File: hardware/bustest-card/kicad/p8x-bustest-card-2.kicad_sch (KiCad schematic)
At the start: 2 parts, among them J1 MABC96R, J2 PROBE

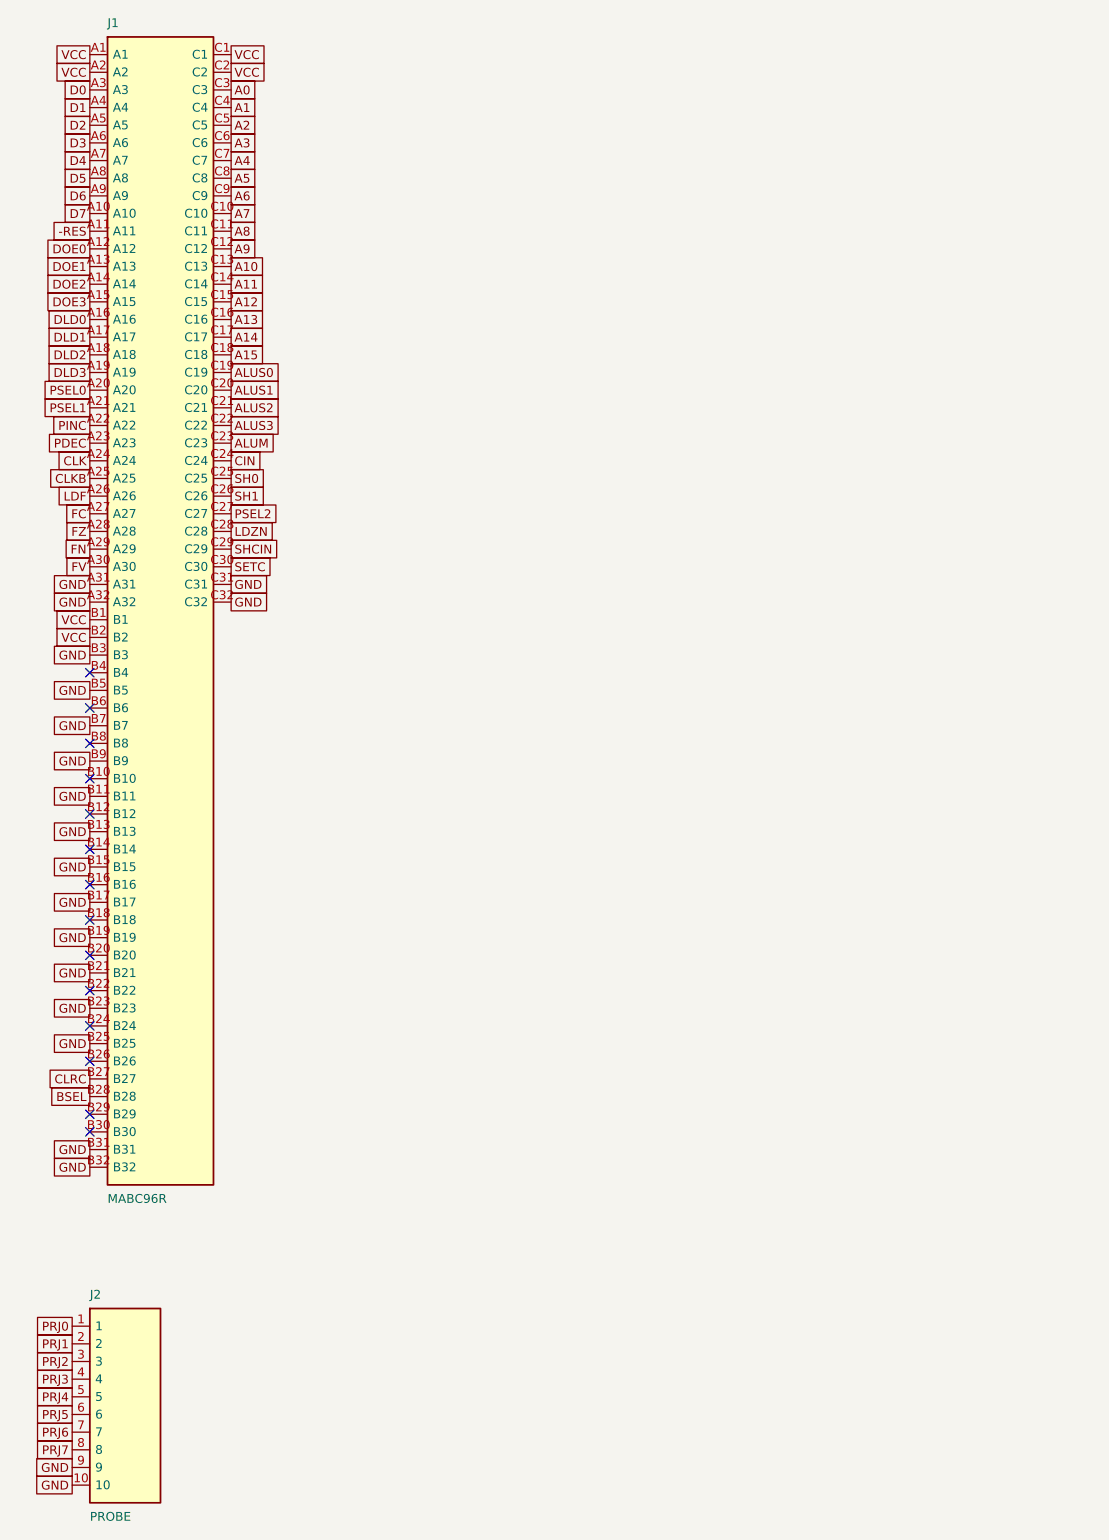
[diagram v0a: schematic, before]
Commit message: feat(sch): draw every P8X card schematic by function
Extend the functional-sheet grouping from the io-card to the control,
regbank, alu, memory, cf, ps2 and bustest cards. functional_sheets now
attaches unnamed glue gates, LEDs, resistors and connectors to the block
they share the most local nets with, so each block lists only its main
parts. A net with two or more pins on a sheet is now wired there even if
it continues elsewhere (its global name label rides on the wire), and
every wire is oriented by drawing side. The regbank gets one pointer per
sheet; the ps2 latches share a sheet with the AVR so the mailbox bus is
drawn. The bustest probe resistors use a straight-order RNISO8DSTR
drawing (the reversed B side forced every wire to cross and the sheet
fell back to labels). build_sch.sh now shows ELK fallbacks and clears old
numbered sheets before a build. All eight netlists match the boards,
ERC 0 errors; the boards change only in footprint link paths.

Co-Authored-By: Claude Opus 5.5 <noreply@anthropic.com>
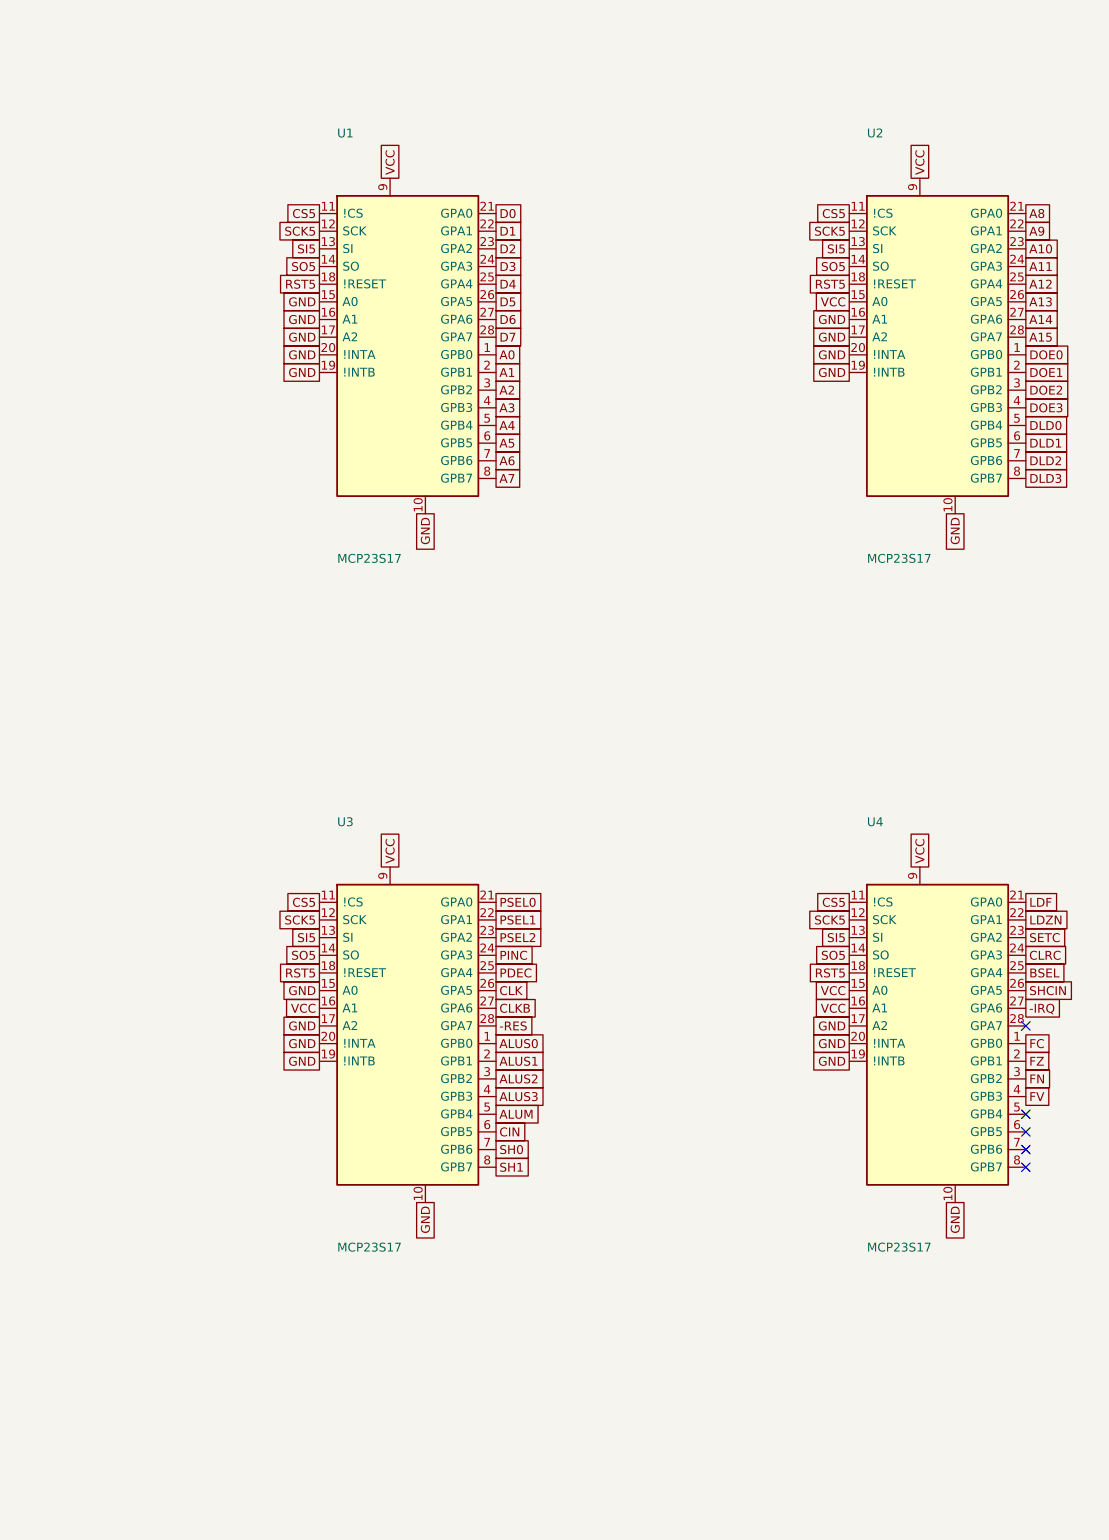
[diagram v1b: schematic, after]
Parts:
- removed J1: MABC96R, Connector_DIN:DIN41612_C_3x32_Male_Horizontal_THT, symbol p8x:DIN96C
- removed J2: PROBE, Connector_PinHeader_2.54mm:PinHeader_1x10_P2.54mm_Vertical, symbol p8x:HDR10
- added U1, U2, U3, U4: MCP23S17, Package_DIP:DIP-28_W7.62mm, symbol p8x:MCP23S17
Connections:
- net -RES: now also U3.28 (GPA7)
- net A0: now also U1.1 (GPB0)
- net A1: now also U1.2 (GPB1)
- net A10: now also U2.23 (GPA2)
- net A11: now also U2.24 (GPA3)
- net A12: now also U2.25 (GPA4)
- net A13: now also U2.26 (GPA5)
- net A14: now also U2.27 (GPA6)
- net A15: now also U2.28 (GPA7)
- net A2: now also U1.3 (GPB2)
- net A3: now also U1.4 (GPB3)
- net A4: now also U1.5 (GPB4)
- net A5: now also U1.6 (GPB5)
- net A6: now also U1.7 (GPB6)
- net A7: now also U1.8 (GPB7)
- net A8: now also U2.21 (GPA0)
- net A9: now also U2.22 (GPA1)
- net ALUM: now also U3.5 (GPB4)
- net ALUS0: now also U3.1 (GPB0)
- net ALUS1: now also U3.2 (GPB1)
- net ALUS2: now also U3.3 (GPB2)
- net ALUS3: now also U3.4 (GPB3)
- net BSEL: now also U4.25 (GPA4)
- net CIN: now also U3.6 (GPB5)
- net CLK: now also U3.26 (GPA5)
- net CLKB: now also U3.27 (GPA6)
- net CLRC: now also U4.24 (GPA3)
- net D0: now also U1.21 (GPA0)
- net D1: now also U1.22 (GPA1)
- net D2: now also U1.23 (GPA2)
- net D3: now also U1.24 (GPA3)
- net D4: now also U1.25 (GPA4)
- net D5: now also U1.26 (GPA5)
- net D6: now also U1.27 (GPA6)
- net D7: now also U1.28 (GPA7)
- net DLD0: now also U2.5 (GPB4)
- net DLD1: now also U2.6 (GPB5)
- net DLD2: now also U2.7 (GPB6)
- net DLD3: now also U2.8 (GPB7)
- net DOE0: now also U2.1 (GPB0)
- net DOE1: now also U2.2 (GPB1)
- net DOE2: now also U2.3 (GPB2)
- net DOE3: now also U2.4 (GPB3)
- net FC: now also U4.1 (GPB0)
- net FN: now also U4.3 (GPB2)
- net FV: now also U4.4 (GPB3)
- net FZ: now also U4.2 (GPB1)
- net GND: now also U1.10, U1.15 (A0), U1.16 (A1), U1.17 (A2), U1.19 (!INTB), U1.20 (!INTA), U2.10, U2.16 (A1), U2.17 (A2), U2.19 (!INTB), U2.20 (!INTA), U3.10, U3.15 (A0), U3.17 (A2), U3.19 (!INTB), U3.20 (!INTA), U4.10, U4.17 (A2), U4.19 (!INTB), U4.20 (!INTA)
- net LDF: now also U4.21 (GPA0)
- net LDZN: now also U4.22 (GPA1)
- net PDEC: now also U3.25 (GPA4)
- net PINC: now also U3.24 (GPA3)
- net PSEL0: now also U3.21 (GPA0)
- net PSEL1: now also U3.22 (GPA1)
- net PSEL2: now also U3.23 (GPA2)
- net SETC: now also U4.23 (GPA2)
- net SH0: now also U3.7 (GPB6)
- net SH1: now also U3.8 (GPB7)
- net SHCIN: now also U4.26 (GPA5)
- net VCC: now also U1.9, U2.15 (A0), U2.9, U3.16 (A1), U3.9, U4.15 (A0), U4.16 (A1), U4.9
- new net -IRQ: U4.27 (GPA6)
- new net CS5: U1.11 (!CS), U2.11 (!CS), U3.11 (!CS), U4.11 (!CS)
- new net RST5: U1.18 (!RESET), U2.18 (!RESET), U3.18 (!RESET), U4.18 (!RESET)
- new net SCK5: U1.12 (SCK), U2.12 (SCK), U3.12 (SCK), U4.12 (SCK)
- new net SI5: U1.13 (SI), U2.13 (SI), U3.13 (SI), U4.13 (SI)
- new net SO5: U1.14 (SO), U2.14 (SO), U3.14 (SO), U4.14 (SO)
- no-connect marks 14 -> 5

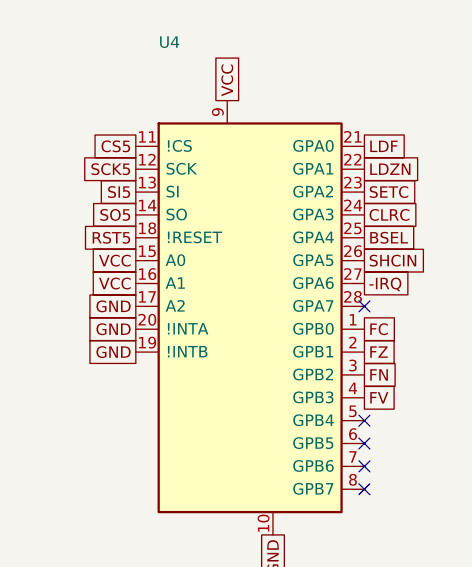
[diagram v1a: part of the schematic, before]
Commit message: fix(bustest): join IRQ and SPARE12-19 to the bus connector
The schematic ERC flagged single-pin labels on the bus test card: U4.GPA6
was named -IRQ while the bus line on B29 is IRQ, and the card's used_bus
set excluded every SPARE* net, so both allocations floated on the routed
board. Name the pin IRQ and map U5 port B to SPARE12-19 (B4-B18, the
design doc's allocation; was SPARE12-17), add the SPARE field to the
firmware table, and re-route the board: DRC 0 unconnected, PASS;
schematic ERC 0 errors, 0 warnings.

Co-Authored-By: Claude Opus 5.5 <noreply@anthropic.com>
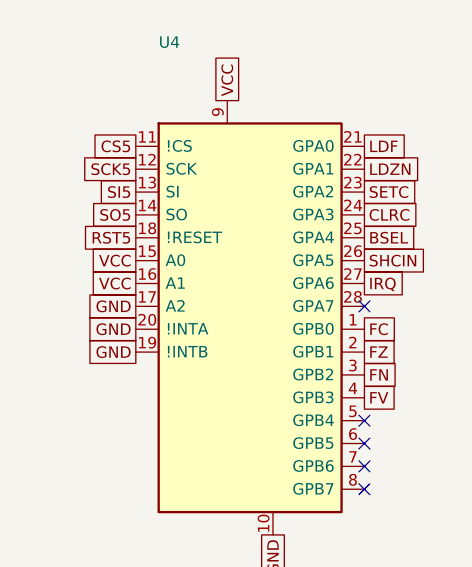
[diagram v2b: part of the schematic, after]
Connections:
- net -IRQ renamed IRQ
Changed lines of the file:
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@@
   (global_label "SHCIN" (shape passive) (at 160.02 167.64 0) (fields_autoplaced yes) (effects (font (size 1.27 1.27)) (justify left))
     (property "Intersheetrefs" "${INTERSHEET_REFS}" (at 160.02 167.64 0) (effects (font (size 1.27 1.27)) hide)))
-  (global_label "-IRQ" (shape passive) (at 160.02 170.18 0) (fields_autoplaced yes) (effects (font (size 1.27 1.27)) (justify left))
+  (global_label "IRQ" (shape passive) (at 160.02 170.18 0) (fields_autoplaced yes) (effects (font (size 1.27 1.27)) (justify left))
     (property "Intersheetrefs" "${INTERSHEET_REFS}" (at 160.02 170.18 0) (effects (font (size 1.27 1.27)) hide)))
   (no_connect (at 160.02 172.72))
